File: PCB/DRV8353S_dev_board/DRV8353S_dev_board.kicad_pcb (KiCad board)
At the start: 4 copper layers, 100 x 85 mm, 143 parts, among them J1 HC_POWER, J2 MOT_LC, J3 SWD, J4 EXT_CMD, J5 PHASE, Q1 BSS84, Q2 CSD19502, Q3 CSD19502, Q4 CSD19502, Q5 CSD19502, Q6 CSD19502, Q7 CSD19502, SW1 B3U, SW2 B3U, SW3 B3U, SW4 B3U, SW5 DIP, U1 ECS-33B, U2 STM32F042K4Ux, U3 MIC5283-3.3ML-TR, U4 MIC5283-5.0ML-TR, U5 DRV8353SM

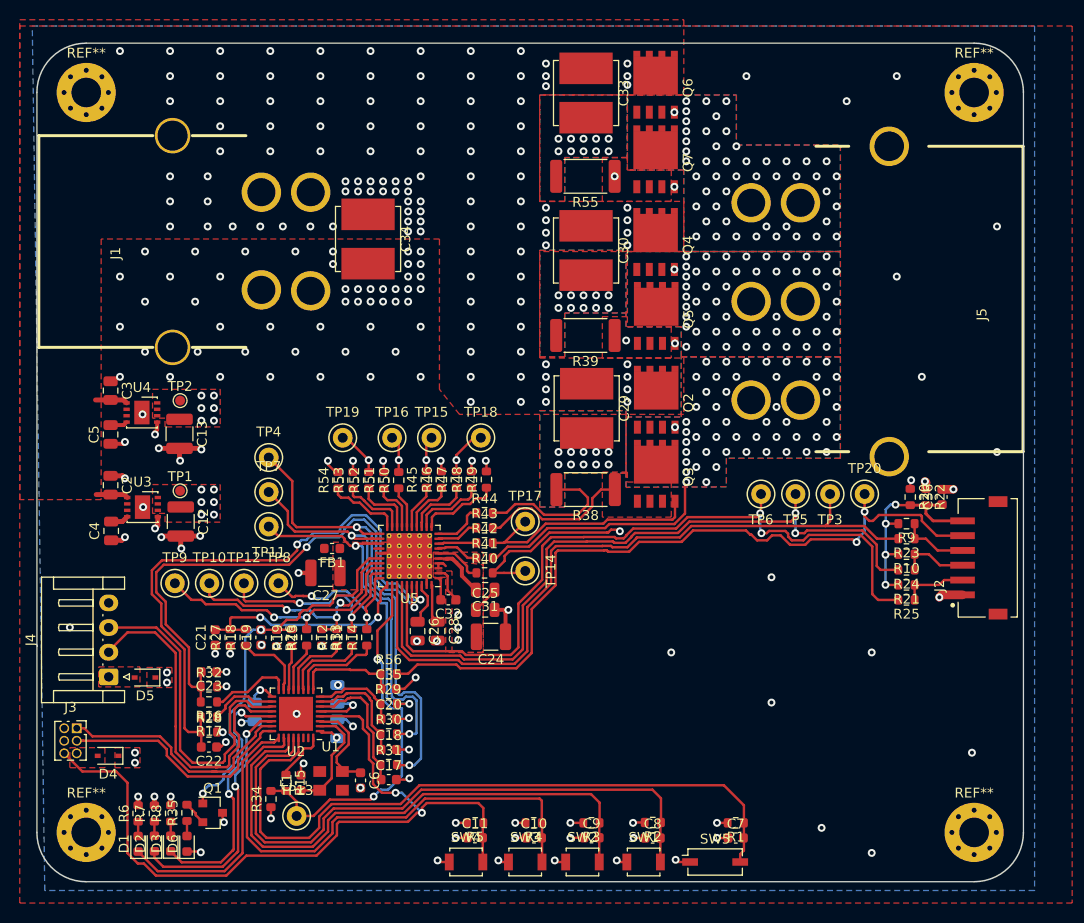
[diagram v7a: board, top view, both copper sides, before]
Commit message: Fixed silkscreen and added BOM
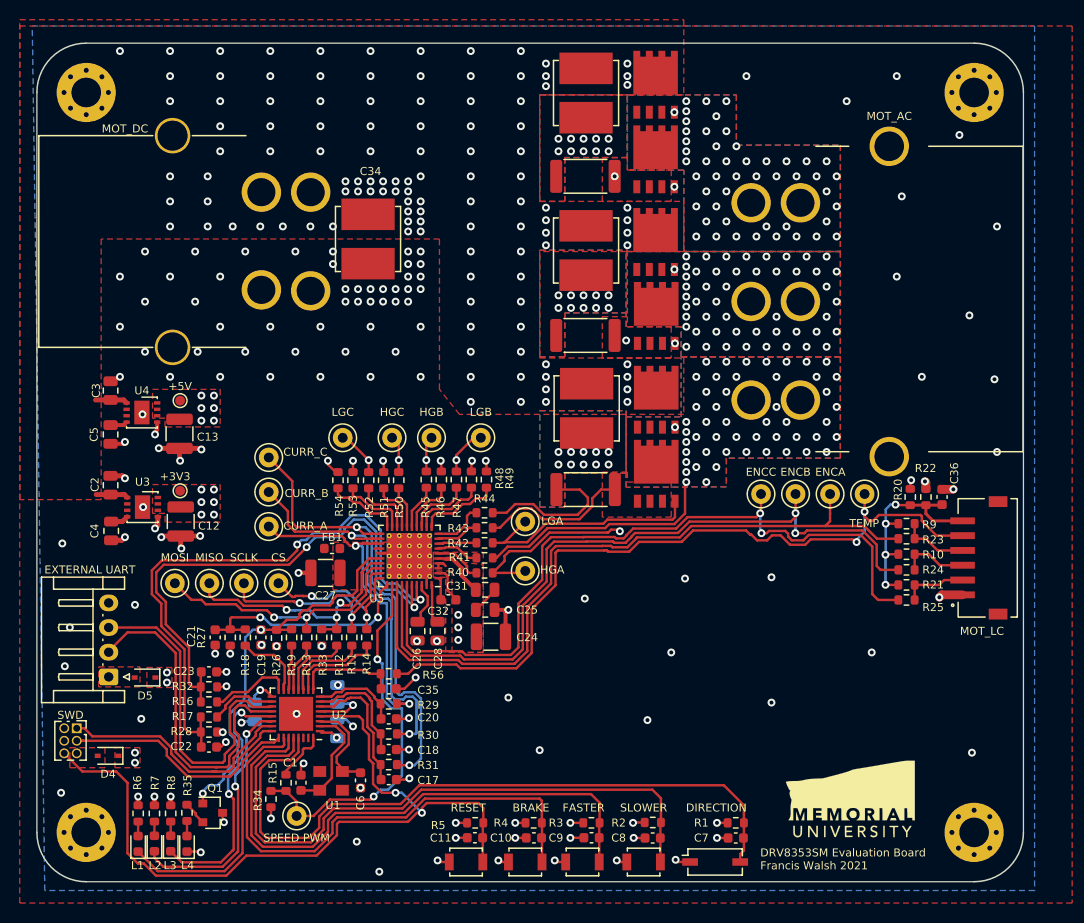
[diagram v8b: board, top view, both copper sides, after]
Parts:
- removed TP4: THT, DRV8353S_dev_board:keystone_5001
- added CURR_C: THT, DRV8353S_dev_board:keystone_5001, F.Cu at (73.5, 92.0)
- added G***: LOGO, DRV8353S_dev_board:school_logo, F.Cu at (132.5, 126.6)
- EXTERNAL UART: renamed from J4
- SPEED PWM: renamed from TP13
- renumbered TP1 to +3V3, TP2 to +5V, SW3 to BRAKE, TP8 to CS, TP11 to CURR_A, TP7 to CURR_B, SW5 to DIRECTION, TP3 to ENCA, TP5 to ENCB, TP6 to ENCC, SW2 to FASTER, TP14 to HGA, TP15 to HGB, TP16 to HGC, D1 to L1, D2 to L2, D3 to L3, D6 to L4, TP17 to LGA, TP18 to LGB, TP19 to LGC, TP10 to MISO, TP9 to MOSI, J5 to MOT_AC, J1 to MOT_DC, J2 to MOT_LC, SW4 to RESET, TP12 to SCLK, SW1 to SLOWER, J3 to SWD, TP20 to TEMP
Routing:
- net GND: vias 177 -> 190
- net +5V: vias 7 -> 8
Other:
- board text added: "DRV8353SM Evaluation Board Francis Walsh 2021"
